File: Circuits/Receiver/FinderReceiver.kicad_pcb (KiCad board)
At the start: 2 copper layers, 50 x 28 mm, 10 parts, among them P1 WRITER, U1 TWE_LITE_SMD

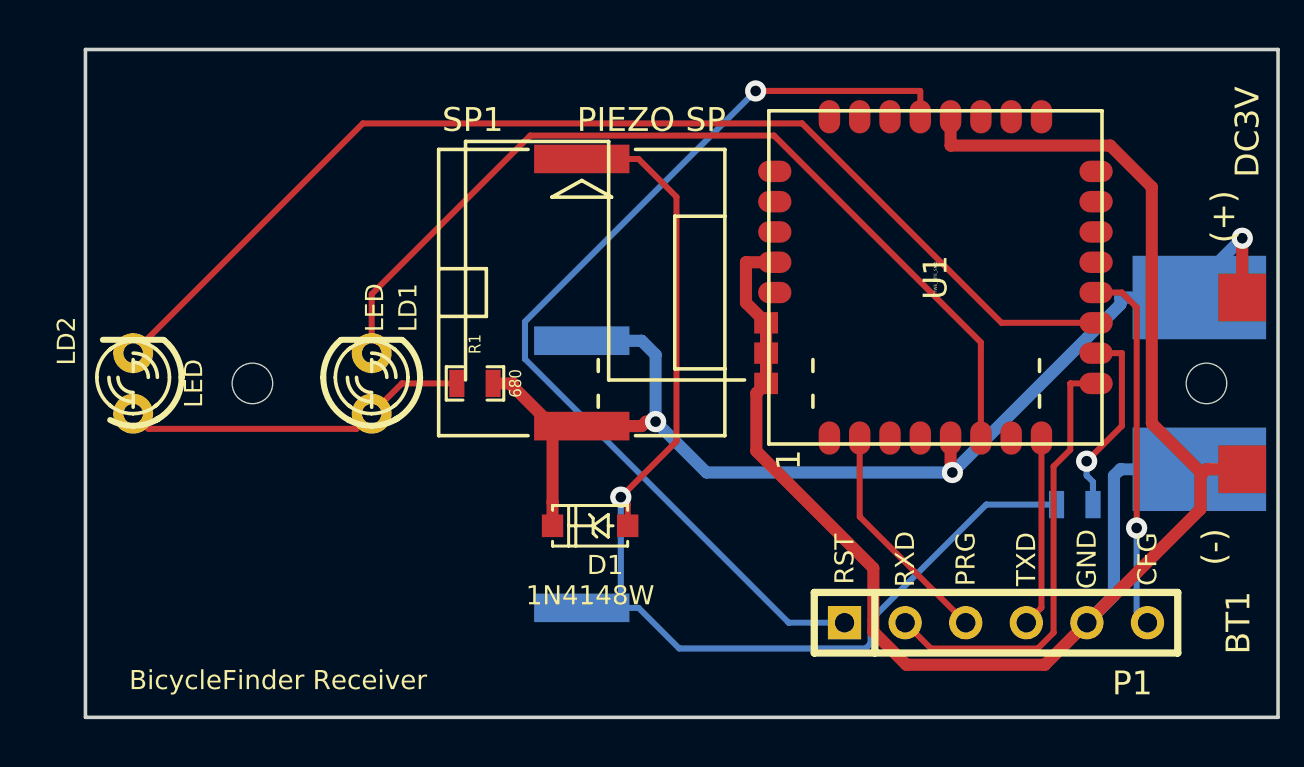
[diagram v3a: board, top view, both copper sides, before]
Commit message: Changed EDLC.
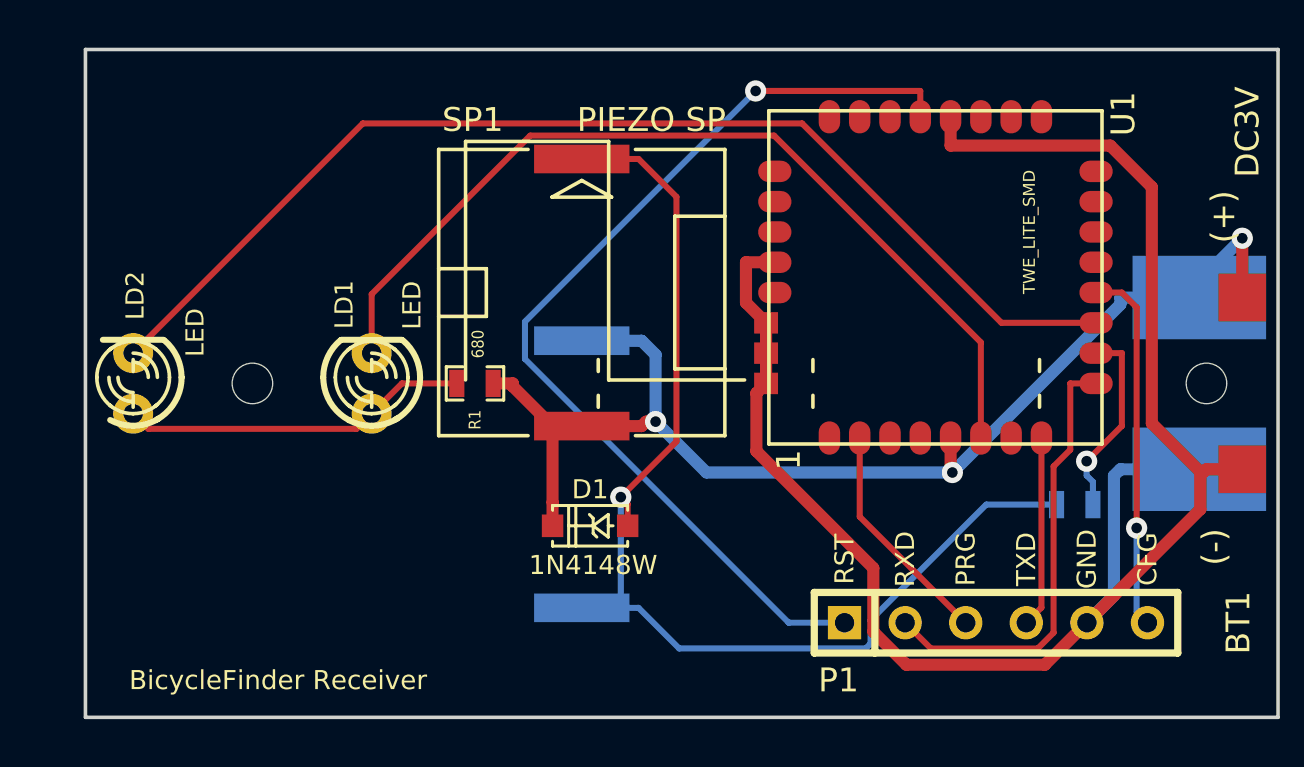
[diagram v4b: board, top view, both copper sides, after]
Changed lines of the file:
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@@
     (links 26)
     (no_connects 0)
-    (area 27.40655 23.516999 79.209001 52.175001)
+    (area 28.550999 23.516999 79.209001 52.175001)
     (thickness 1)
     (drawings 5)
@@
     (descr "LED 3mm - Lead pitch 100mil (2,54mm)")
     (tags "LED led 3mm 3MM 100mil 2,54mm")
-    (fp_text reference LD2 (at 1.778 -2.794 90) (layer F.SilkS)
+    (fp_text reference LD2 (at 3.683 0.0826 90) (layer F.SilkS)
       (effects (font (size 0.762 0.762) (thickness 0.0889)))
     )
-    (fp_text value LED (at 0 2.54 90) (layer F.SilkS)
+    (fp_text value LED (at 2.1336 2.5972 90) (layer F.SilkS)
       (effects (font (size 0.762 0.762) (thickness 0.0889)))
     )
@@
     (at 45.212 37.846 180)
     (attr smd)
-    (fp_text reference R1 (at 0 1.651 270) (layer F.SilkS)
+    (fp_text reference R1 (at 0 -1.524 270) (layer F.SilkS)
       (effects (font (size 0.50038 0.4572) (thickness 0.1143)))
     )
-    (fp_text value 680 (at -1.69926 0 270) (layer F.SilkS)
+    (fp_text value 680 (at -0.127 1.651 270) (layer F.SilkS)
       (effects (font (size 0.508 0.4572) (thickness 0.1143)))
     )
@@
     (tags "1N4148 SOD123")
     (attr smd)
-    (fp_text reference D1 (at -0.635 -1.651 180) (layer F.SilkS)
+    (fp_text reference D1 (at 0 1.524 180) (layer F.SilkS)
       (effects (font (size 0.8 0.8) (thickness 0.11938)))
     )
-    (fp_text value 1N4148W (at 0 -2.921 180) (layer F.SilkS)
+    (fp_text value 1N4148W (at -0.127 -1.651 180) (layer F.SilkS)
       (effects (font (size 0.8 0.8) (thickness 0.11938)))
     )
@@
     (descr "LED 3mm - Lead pitch 100mil (2,54mm)")
     (tags "LED led 3mm 3MM 100mil 2,54mm")
-    (fp_text reference LD1 (at 3.175 1.524 90) (layer F.SilkS)
+    (fp_text reference LD1 (at 3.302 -1.1544 90) (layer F.SilkS)
       (effects (font (size 0.762 0.762) (thickness 0.0889)))
     )
-    (fp_text value LED (at 3.175 0.127 90) (layer F.SilkS)
+    (fp_text value LED (at 3.2766 1.6904 90) (layer F.SilkS)
       (effects (font (size 0.762 0.762) (thickness 0.0889)))
     )
@@
   (module TWE-001L-SMD-noNTH (layer F.Cu)
     (at 64.516 33.401 90)
-    (fp_text reference U1 (at 0 0 90) (layer F.SilkS)
+    (fp_text reference U1 (at 6.858 7.874 90) (layer F.SilkS)
       (effects (font (size 1 1) (thickness 0.15)))
     )
-    (fp_text value TWE_LITE_SMD (at 0 0 90) (layer F.SilkS)
-      (effects (font (size 0.127 0.127) (thickness 0.000001)))
+    (fp_text value TWE_LITE_SMD (at 1.905 3.937 90) (layer F.SilkS)
+      (effects (font (size 0.5 0.5) (thickness 0.08)))
     )
     (fp_text user 1 (at -7.65 -6.15 90) (layer F.SilkS)
@@
     (descr "Connecteur 6 pins")
     (tags "CONN DEV")
-    (fp_text reference P1 (at 6.985 2.54) (layer F.SilkS)
+    (fp_text reference P1 (at -5.334 2.413) (layer F.SilkS)
       (effects (font (size 1 1) (thickness 0.2)))
     )
@@
   (segment (start 71.251 37.846) (end 70.1697 37.846) (width 0.254) (layer F.Cu) (net 7))
   (via (at 70.8555 41.1071) (size 0.889) (layers F.Cu B.Cu) (net 8))
+  (segment (start 72.3323 36.576) (end 72.3323 39.6303) (width 0.254) (layer F.Cu) (net 8))
+  (segment (start 72.3323 39.6303) (end 70.8555 41.1071) (width 0.254) (layer F.Cu) (net 8))
+  (segment (start 71.12 41.9732) (end 70.8555 41.7087) (width 0.254) (layer B.Cu) (net 8))
+  (segment (start 70.8555 41.7087) (end 70.8555 41.1071) (width 0.254) (layer B.Cu) (net 8))
+  (segment (start 71.12 42.926) (end 71.12 41.9732) (width 0.254) (layer B.Cu) (net 8))
   (segment (start 71.251 36.576) (end 72.3323 36.576) (width 0.254) (layer F.Cu) (net 8))
-  (segment (start 71.12 42.926) (end 71.12 41.9732) (width 0.254) (layer B.Cu) (net 8))
-  (segment (start 70.8555 41.7087) (end 70.8555 41.1071) (width 0.254) (layer B.Cu) (net 8))
-  (segment (start 71.12 41.9732) (end 70.8555 41.7087) (width 0.254) (layer B.Cu) (net 8))
-  (segment (start 72.3323 39.6303) (end 70.8555 41.1071) (width 0.254) (layer F.Cu) (net 8))
-  (segment (start 72.3323 36.576) (end 72.3323 39.6303) (width 0.254) (layer F.Cu) (net 8))
   (via (at 51.3245 42.6127) (size 0.889) (layers F.Cu B.Cu) (net 9))
   (segment (start 66.6456 42.926) (end 69.596 42.926) (width 0.254) (layer B.Cu) (net 9))

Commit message: Reload net list.
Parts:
- BT1: value DC3V -> BATTERY
- U1: footprint TWE-001L-SMD-noNTH -> TWE-001L-NC7
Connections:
- U1 pad 22: (no net) -> VCC
- U1 pad 23: (no net) -> VCC
- U1 pad 24: (no net) -> VCC
- U1 pad 25: (no net) -> VCC
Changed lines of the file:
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@@
 (kicad_pcb (version 3) (host pcbnew "(2013-07-07 BZR 4022)-stable")
   (general
-    (links 26)
-    (no_connects 0)
-    (area 28.550999 23.516999 79.209001 52.175001)
+    (links 30)
+    (no_connects 4)
+    (area 28.550999 23.087112 79.209001 52.175001)
     (thickness 1)
     (drawings 5)
@@
     (visible_elements 7FFFFFFF)
     (pcbplotparams
-      (layerselection 3178497)
+      (layerselection 284196865)
       (usegerberextensions true)
       (excludeedgelayer true)
@@
       (psa4output false)
       (plotreference true)
-      (plotvalue true)
+      (plotvalue false)
       (plotothertext true)
       (plotinvisibletext false)
@@
       (outputformat 1)
       (mirror false)
-      (drillshape 1)
+      (drillshape 0)
       (scaleselection 1)
-      (outputdirectory ""))
+      (outputdirectory gerber/))
   )
   (net 0 "")
@@
       (effects (font (size 1 1) (thickness 0.15)))
     )
-    (fp_text value DC3V (at 21.717 -10.541 90) (layer F.SilkS)
+    (fp_text value BATTERY (at 21.717 -10.541 90) (layer F.SilkS)
       (effects (font (size 1 1) (thickness 0.15)))
     )
@@
     )
   )
-  (module TWE-001L-SMD-noNTH (layer F.Cu)
+  (module WRITER-6P (layer F.Cu)
+    (at 65.786 47.879)
+    (descr "Connecteur 6 pins")
+    (tags "CONN DEV")
+    (fp_text reference P1 (at -5.334 2.413) (layer F.SilkS)
+      (effects (font (size 1 1) (thickness 0.2)))
+    )
+    (fp_text value WRITER (at 0 2.5) (layer F.SilkS) hide
+      (effects (font (size 1 1) (thickness 0.2)))
+    )
+    (fp_text user CFG (at 7.62 -2.667 90) (layer F.SilkS)
+      (effects (font (size 0.8 0.8) (thickness 0.15)))
+    )
+    (fp_text user GND (at 5.08 -2.667 90) (layer F.SilkS)
+      (effects (font (size 0.8 0.8) (thickness 0.15)))
+    )
+    (fp_text user TXD (at 2.54 -2.667 90) (layer F.SilkS)
+      (effects (font (size 0.8 0.8) (thickness 0.15)))
+    )
+    (fp_text user PRG (at 0 -2.667 90) (layer F.SilkS)
+      (effects (font (size 0.8 0.8) (thickness 0.15)))
+    )
+    (fp_text user RXD (at -2.54 -2.667 90) (layer F.SilkS)
+      (effects (font (size 0.8 0.8) (thickness 0.15)))
+    )
+    (fp_text user RST (at -5.08 -2.667 90) (layer F.SilkS)
+      (effects (font (size 0.8 0.8) (thickness 0.15)))
+    )
+    (fp_line (start -6.35 -1.27) (end 8.89 -1.27) (layer F.SilkS) (width 0.3048))
+    (fp_line (start 8.89 -1.27) (end 8.89 1.27) (layer F.SilkS) (width 0.3048))
+    (fp_line (start 8.89 1.27) (end -6.35 1.27) (layer F.SilkS) (width 0.3048))
+    (fp_line (start -3.81 1.27) (end -3.81 -1.27) (layer F.SilkS) (width 0.3048))
+    (fp_line (start -6.35 1.27) (end -6.35 1.27) (layer F.SilkS) (width 0.3048))
+    (fp_line (start -6.35 1.27) (end -6.35 -1.27) (layer F.SilkS) (width 0.3048))
+    (pad 1 thru_hole rect (at -5.08 0) (size 1.397 1.397) (drill 0.8128)
+      (layers *.Cu *.SilkS *.Mask)
+      (net 6 /RST)
+    )
+    (pad 2 thru_hole circle (at -2.54 0) (size 1.397 1.397) (drill 0.8128)
+      (layers *.Cu *.SilkS *.Mask)
+      (net 7 /RXD)
+    )
+    (pad 3 thru_hole circle (at 0 0) (size 1.397 1.397) (drill 0.8128)
+      (layers *.Cu *.SilkS *.Mask)
+      (net 5 /PRG)
+    )
+    (pad 4 thru_hole circle (at 2.54 0) (size 1.397 1.397) (drill 0.8128)
+      (layers *.Cu *.SilkS *.Mask)
+      (net 10 /TXD)
+    )
+    (pad 5 thru_hole circle (at 5.08 0) (size 1.397 1.397) (drill 0.8128)
+      (layers *.Cu *.SilkS *.Mask)
+      (net 11 GND)
+    )
+    (pad 6 thru_hole circle (at 7.62 0) (size 1.397 1.397) (drill 0.8128)
+      (layers *.Cu *.SilkS *.Mask)
+      (net 1 /CFG)
+    )
+  )
+  (module TWE-001L-NC7 (layer F.Cu)
     (at 64.516 33.401 90)
-    (fp_text reference U1 (at 6.858 7.874 90) (layer F.SilkS)
+    (fp_text reference U1 (at 0.1 -9.35 90) (layer F.SilkS)
       (effects (font (size 1 1) (thickness 0.15)))
     )
-    (fp_text value TWE_LITE_SMD (at 1.905 3.937 90) (layer F.SilkS)
-      (effects (font (size 0.5 0.5) (thickness 0.08)))
-    )
+    (fp_text value TWE_LITE_SMD (at 0 0.85 90) (layer F.SilkS)
+      (effects (font (size 0.127 0.127) (thickness 0.000001)))
+    )
+    (fp_line (start -0.5 0) (end -0.2 0) (layer F.SilkS) (width 0.15))
+    (fp_line (start 0 -0.5) (end 0 -0.2) (layer F.SilkS) (width 0.15))
+    (fp_line (start 0 0.5) (end 0 0.2) (layer F.SilkS) (width 0.15))
+    (fp_line (start 0.2 0) (end 0.5 0) (layer F.SilkS) (width 0.15))
     (fp_text user 1 (at -7.65 -6.15 90) (layer F.SilkS)
       (effects (font (size 1 1) (thickness 0.15)))
     )
+    (fp_arc (start -4.95 -4.25) (end -4.95 -3.5) (angle 90) (layer Edge.Cuts) (width 0.15))
+    (fp_line (start -5.7 -4.25) (end -5.7 -5.85) (layer Edge.Cuts) (width 0.15))
+    (fp_arc (start -4.95 -5.85) (end -5.7 -5.85) (angle 90) (layer Edge.Cuts) (width 0.15))
+    (fp_line (start -2.15 -6.6) (end -4.95 -6.6) (layer Edge.Cuts) (width 0.15))
+    (fp_arc (start -2.15 -5.85) (end -2.15 -6.6) (angle 90) (layer Edge.Cuts) (width 0.15))
+    (fp_line (start -1.4 -5.85) (end -1.4 -4.25) (layer Edge.Cuts) (width 0.15))
+    (fp_arc (start -2.15 -4.25) (end -1.4 -4.25) (angle 90) (layer Edge.Cuts) (width 0.15))
+    (fp_line (start -2.15 -3.5) (end -4.95 -3.5) (layer Edge.Cuts) (width 0.15))
     (fp_line (start -6.985 -6.985) (end -6.985 6.985) (layer F.SilkS) (width 0.15))
     (fp_line (start -6.985 6.985) (end 6.985 6.985) (layer F.SilkS) (width 0.15))
@@
     (pad 22 smd oval (at 6.735 -1.905 180) (size 0.9 1.4)
       (layers F.Cu F.Paste F.Mask)
+      (net 12 VCC)
     )
     (pad 23 smd oval (at 6.735 -3.175 180) (size 0.9 1.4)
       (layers F.Cu F.Paste F.Mask)
+      (net 12 VCC)
     )
     (pad 24 smd oval (at 6.735 -4.445 180) (size 0.9 1.4)
       (layers F.Cu F.Paste F.Mask)
+      (net 12 VCC)
     )
     (pad 25 smd oval (at 4.445 -6.735 90) (size 0.9 1.4)
       (layers F.Cu F.Paste F.Mask)
+      (net 12 VCC)
     )
     (pad 26 smd oval (at 3.175 -6.735 90) (size 0.9 1.4)
@@
     )
   )
-  (module WRITER-6P (layer F.Cu)
-    (at 65.786 47.879)
-    (descr "Connecteur 6 pins")
-    (tags "CONN DEV")
-    (fp_text reference P1 (at -5.334 2.413) (layer F.SilkS)
-      (effects (font (size 1 1) (thickness 0.2)))
-    )
-    (fp_text value WRITER (at 0 2.5) (layer F.SilkS) hide
-      (effects (font (size 1 1) (thickness 0.2)))
-    )
-    (fp_text user CFG (at 7.62 -2.667 90) (layer F.SilkS)
-      (effects (font (size 0.8 0.8) (thickness 0.15)))
-    )
-    (fp_text user GND (at 5.08 -2.667 90) (layer F.SilkS)
-      (effects (font (size 0.8 0.8) (thickness 0.15)))
-    )
-    (fp_text user TXD (at 2.54 -2.667 90) (layer F.SilkS)
-      (effects (font (size 0.8 0.8) (thickness 0.15)))
-    )
-    (fp_text user PRG (at 0 -2.667 90) (layer F.SilkS)
-      (effects (font (size 0.8 0.8) (thickness 0.15)))
-    )
-    (fp_text user RXD (at -2.54 -2.667 90) (layer F.SilkS)
-      (effects (font (size 0.8 0.8) (thickness 0.15)))
-    )
-    (fp_text user RST (at -5.08 -2.667 90) (layer F.SilkS)
-      (effects (font (size 0.8 0.8) (thickness 0.15)))
-    )
-    (fp_line (start -6.35 -1.27) (end 8.89 -1.27) (layer F.SilkS) (width 0.3048))
-    (fp_line (start 8.89 -1.27) (end 8.89 1.27) (layer F.SilkS) (width 0.3048))
-    (fp_line (start 8.89 1.27) (end -6.35 1.27) (layer F.SilkS) (width 0.3048))
-    (fp_line (start -3.81 1.27) (end -3.81 -1.27) (layer F.SilkS) (width 0.3048))
-    (fp_line (start -6.35 1.27) (end -6.35 1.27) (layer F.SilkS) (width 0.3048))
-    (fp_line (start -6.35 1.27) (end -6.35 -1.27) (layer F.SilkS) (width 0.3048))
-    (pad 1 thru_hole rect (at -5.08 0) (size 1.397 1.397) (drill 0.8128)
-      (layers *.Cu *.SilkS *.Mask)
-      (net 6 /RST)
-    )
-    (pad 2 thru_hole circle (at -2.54 0) (size 1.397 1.397) (drill 0.8128)
-      (layers *.Cu *.SilkS *.Mask)
-      (net 7 /RXD)
-    )
-    (pad 3 thru_hole circle (at 0 0) (size 1.397 1.397) (drill 0.8128)
-      (layers *.Cu *.SilkS *.Mask)
-      (net 5 /PRG)
-    )
-    (pad 4 thru_hole circle (at 2.54 0) (size 1.397 1.397) (drill 0.8128)
-      (layers *.Cu *.SilkS *.Mask)
-      (net 10 /TXD)
-    )
-    (pad 5 thru_hole circle (at 5.08 0) (size 1.397 1.397) (drill 0.8128)
-      (layers *.Cu *.SilkS *.Mask)
-      (net 11 GND)
-    )
-    (pad 6 thru_hole circle (at 7.62 0) (size 1.397 1.397) (drill 0.8128)
-      (layers *.Cu *.SilkS *.Mask)
-      (net 1 /CFG)
-    )
-  )

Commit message: Modified some connections.
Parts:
- BT1: value BATTERY -> DC3V
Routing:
- net /RST: track 41.2 -> 76.3 mm, vias 1 -> 0
- net VCC: track 52.1 -> 75.2 mm
- net GND: track 73.1 -> 63.2 mm
- net /DO3: track 38.4 -> 29.9 mm, vias 0 -> 1
- net /DO4: track 47.8 -> 54.6 mm
- net /SPK: track 48.0 -> 48.8 mm
- net /CFG: vias 1 -> 0

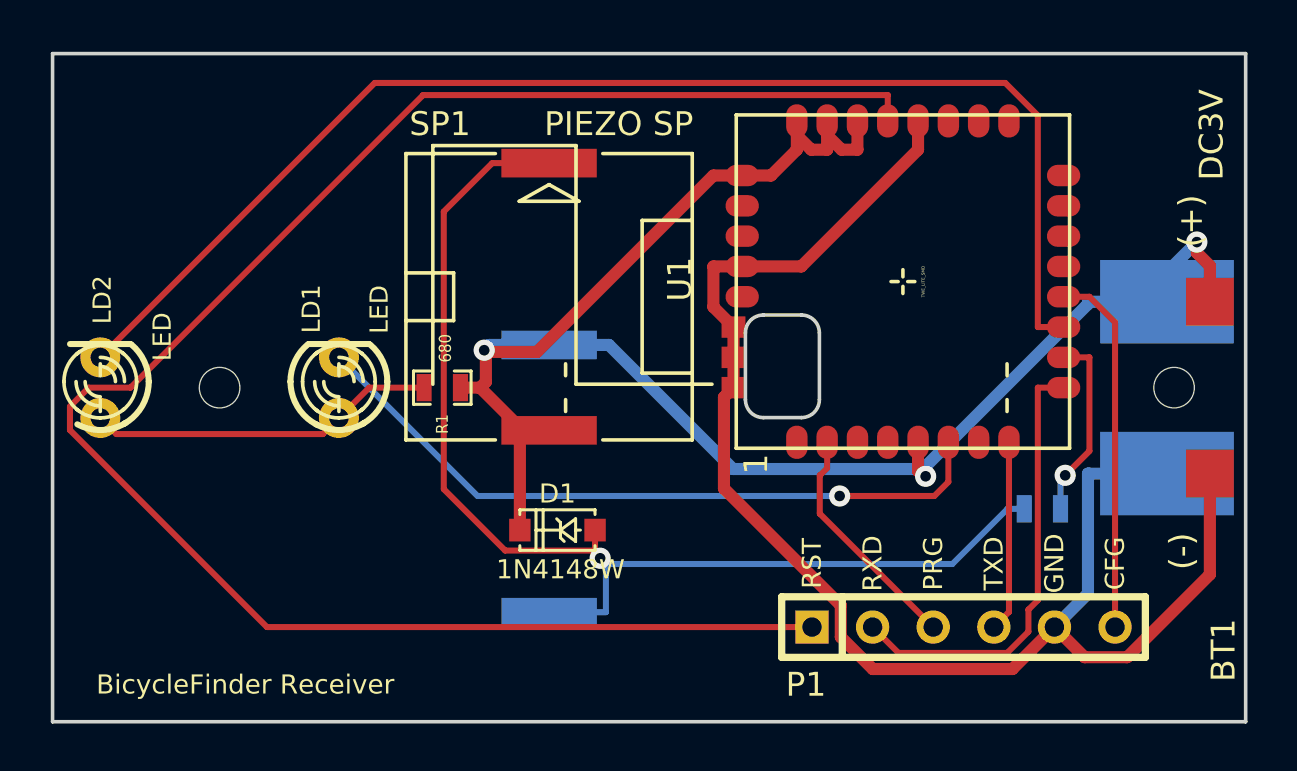
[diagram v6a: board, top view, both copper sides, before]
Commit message: Fixed: Sound output is connected to PWM1.
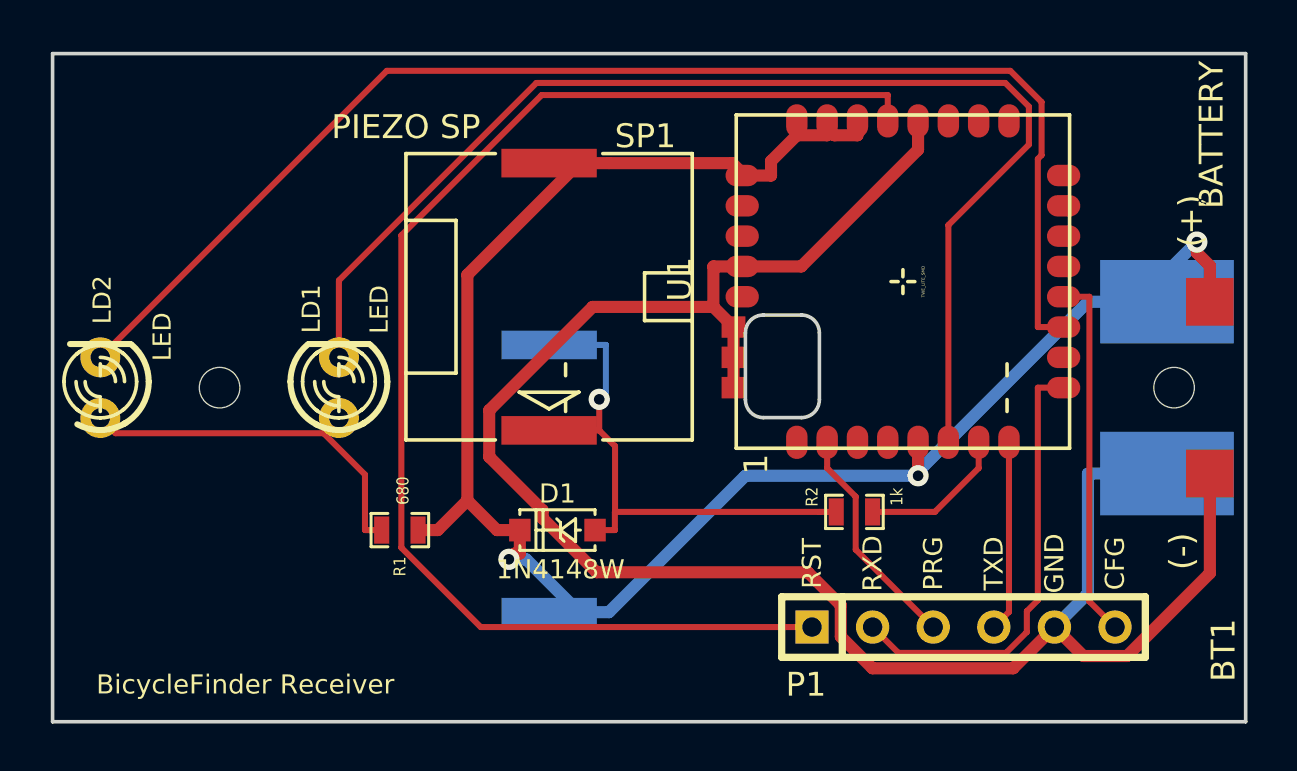
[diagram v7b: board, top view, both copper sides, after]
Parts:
- BT1: value DC3V -> BATTERY
- R2: moved to F.Cu
- moved R2 7.88 mm to (62.5, 43.1)
- moved R1 6.23 mm to (43.4, 43.8)
- turned SP1 to 270 degrees
- turned SP2 to 90 degrees
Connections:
- U1 pad 10: /SOUND -> (no net)
- U1 pad 7: (no net) -> /SOUND
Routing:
- net /SPK: track 48.8 -> 22.7 mm
- net /DO3: track 29.9 -> 51.4 mm, vias 1 -> 0
- net /RST: track 76.3 -> 55.6 mm
- net GND: track 63.2 -> 82.4 mm
- net VCC: track 75.2 -> 81.5 mm
- net /SOUND: track 7.93 -> 6.29 mm, vias 1 -> 0
- net /LED: track 14.7 -> 16.0 mm
- net /DO4: track 54.6 -> 55.5 mm
